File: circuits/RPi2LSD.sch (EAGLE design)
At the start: 36 parts, among them K1 PIN20X2

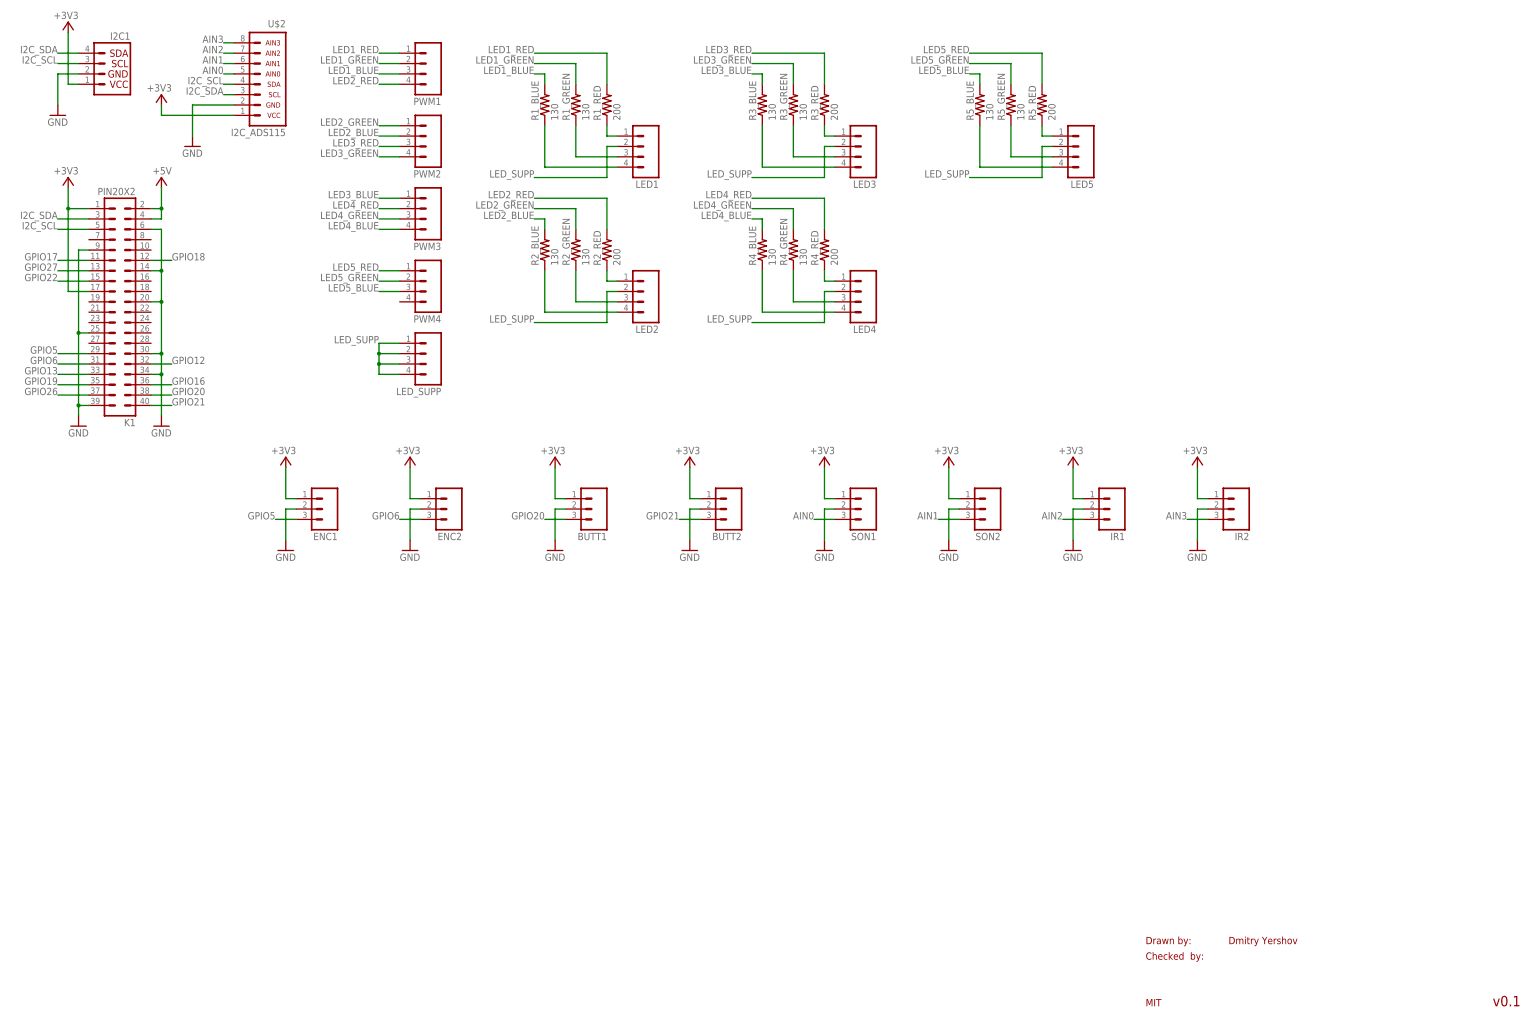
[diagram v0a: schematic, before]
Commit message: Updated circuit boards. Use .brd file for OSH jobs.
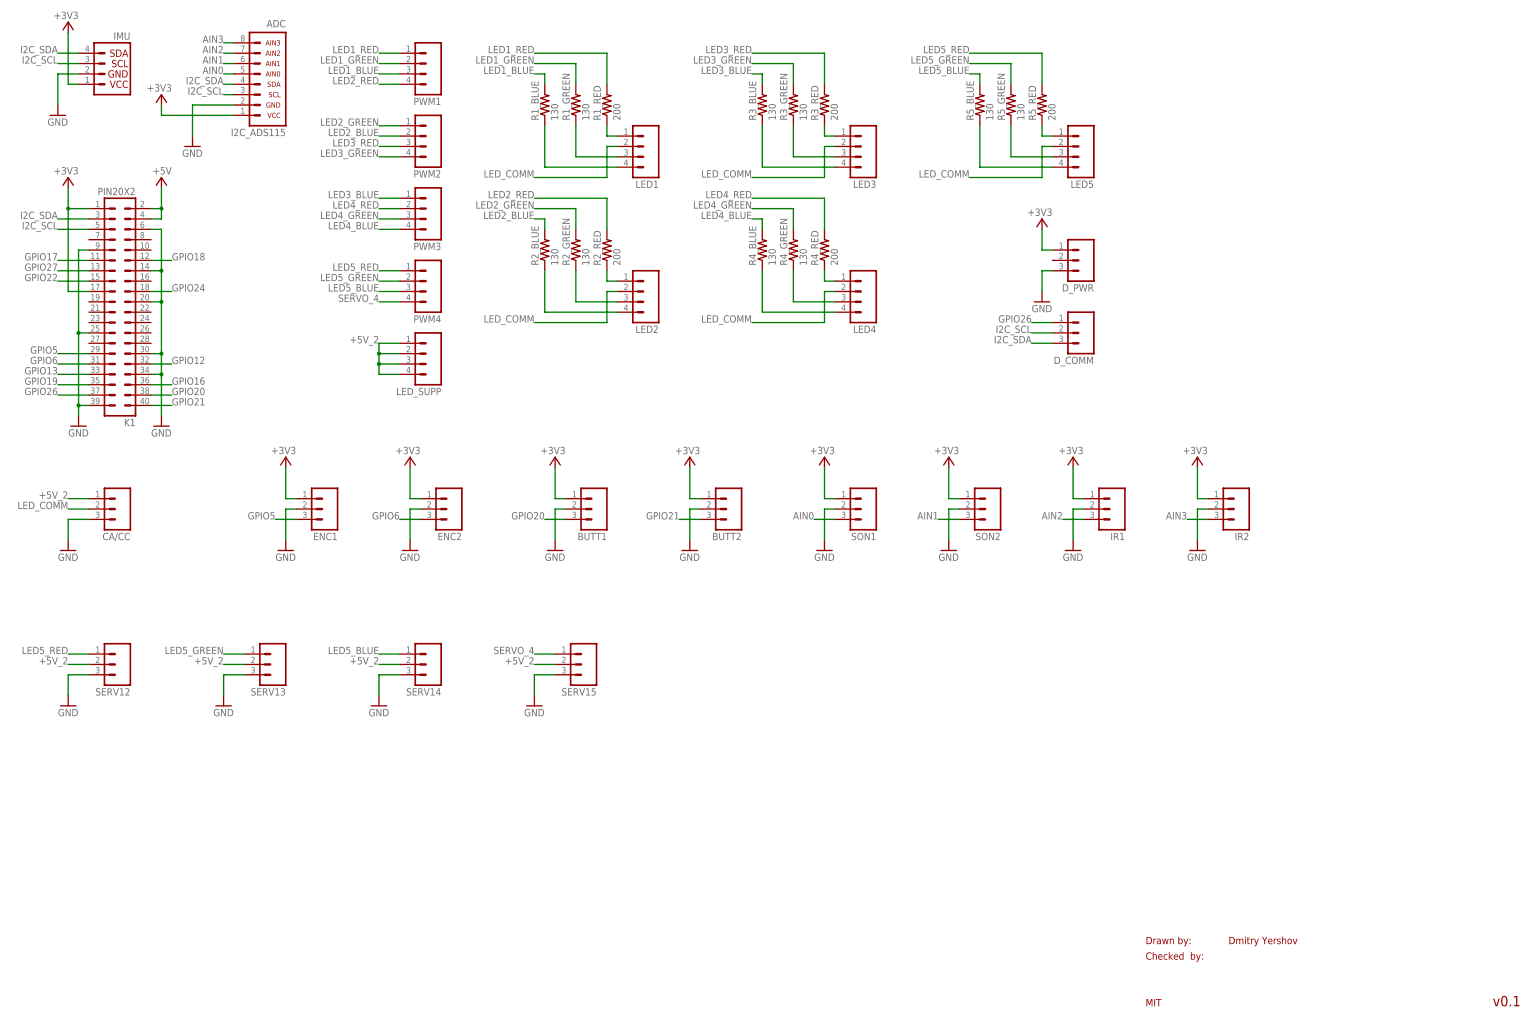
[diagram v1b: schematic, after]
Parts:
- added CA/CC, D_COMM, D_PWR, SERV12, SERV13, SERV14, SERV15: (no value), cambridge_garage_electronics:M03PTH
- BUTT1, BUTT2, ENC1, ENC2, IR1, IR2, SON1, SON2: device SparkFun-Connectors:M03PTH -> cambridge_garage_electronics:M03PTH
- R1_BLUE, R1_GREEN, R1_RED, R2_BLUE, R2_GREEN, R2_RED, R3_BLUE, R3_GREEN, R3_RED, R4_BLUE, R4_GREEN, R4_RED, R5_BLUE, R5_GREEN, R5_RED: device adafruit:R-US_0207/7 -> adafruit:R-US_0207/9
- renumbered I2C1 to IMU, U$2 to ADC
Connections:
- removed net LED_SUPP: LED1.2, LED2.2, LED3.2, LED4.2, LED5.2, LED_SUPP.1, LED_SUPP.2, LED_SUPP.3, LED_SUPP.4
- new net +5V_2: CA/CC.1, LED_SUPP.1, LED_SUPP.2, LED_SUPP.3, LED_SUPP.4, SERV12.2, SERV13.2, SERV14.2, SERV15.2
- new net GPIO24: K1.18
- new net LED_COMM: CA/CC.2, LED1.2, LED2.2, LED3.2, LED4.2, LED5.2
- new net SERVO_4: PWM4.4, SERV15.1
- net +3V3: now also D_PWR.1
- net GND: now also CA/CC.3, D_PWR.3, SERV12.3, SERV13.3, SERV14.3, SERV15.3
- net GPIO26: now also D_COMM.1
- net I2C_SCL: now also ADC.3, D_COMM.2; no longer ADC.4
- net I2C_SDA: now also ADC.4, D_COMM.3; no longer ADC.3
- net LED5_BLUE: now also SERV14.1
- net LED5_GREEN: now also SERV13.1
- net LED5_RED: now also SERV12.1
